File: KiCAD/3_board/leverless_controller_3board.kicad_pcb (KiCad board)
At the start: 2 copper layers, 208.5 x 127.2 mm, 110 parts, among them J1 USB_C_Receptacle_USB2.0_14P, J2 Conn_01x03_Socket, SW1 Memory Reset, SW10_SHARE1 SW_Push, SW11_START1 SW_Push, SW12_THROW1 SW_Push, SW14_PS1 SW_Push, SW15_TOUCHPAD1 SW_Push, SW16_SPACE1 SW_Push, SW17_W1 SW_Push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

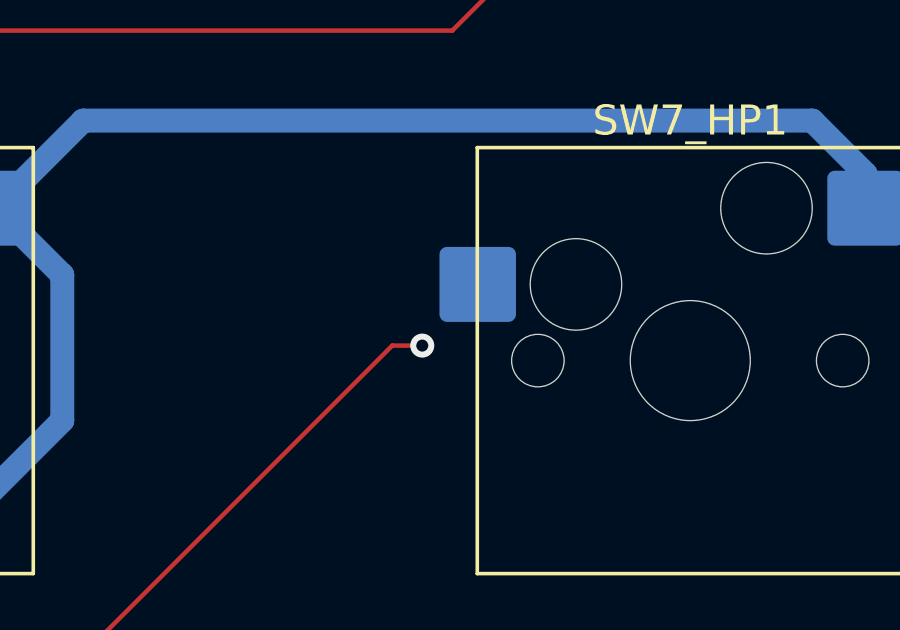
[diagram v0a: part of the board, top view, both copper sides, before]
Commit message: Fix missing connection to HP
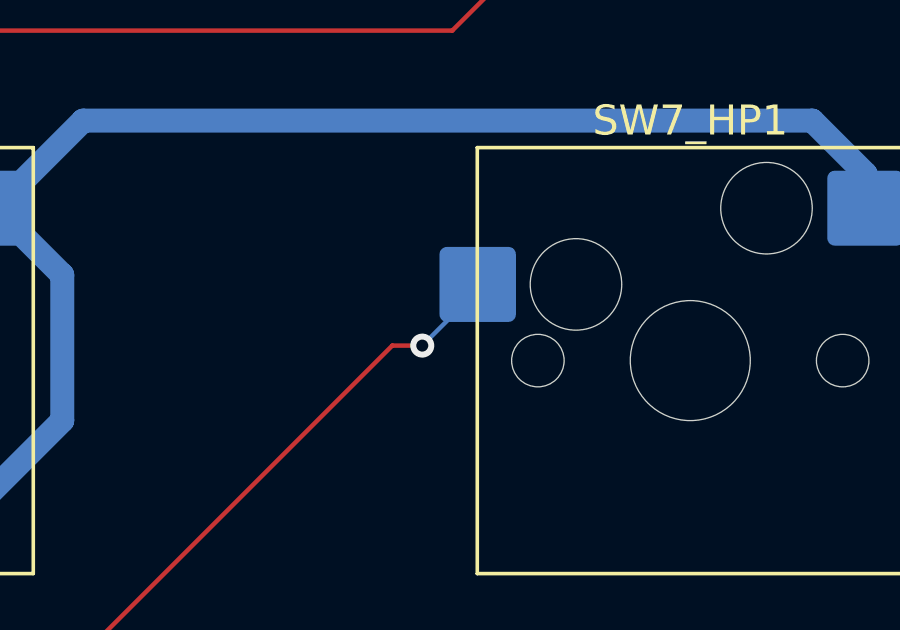
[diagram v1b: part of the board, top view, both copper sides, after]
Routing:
- net /Buttons/R1: track 78.3 -> 81.1 mm
